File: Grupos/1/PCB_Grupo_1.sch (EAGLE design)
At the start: 45 parts, among them T1 2N7002-7-F, T2 2N7002-7-F, U1 MAX3221ECPWR, U2 ST1S14PHR, U3 MAX31855KASA+T

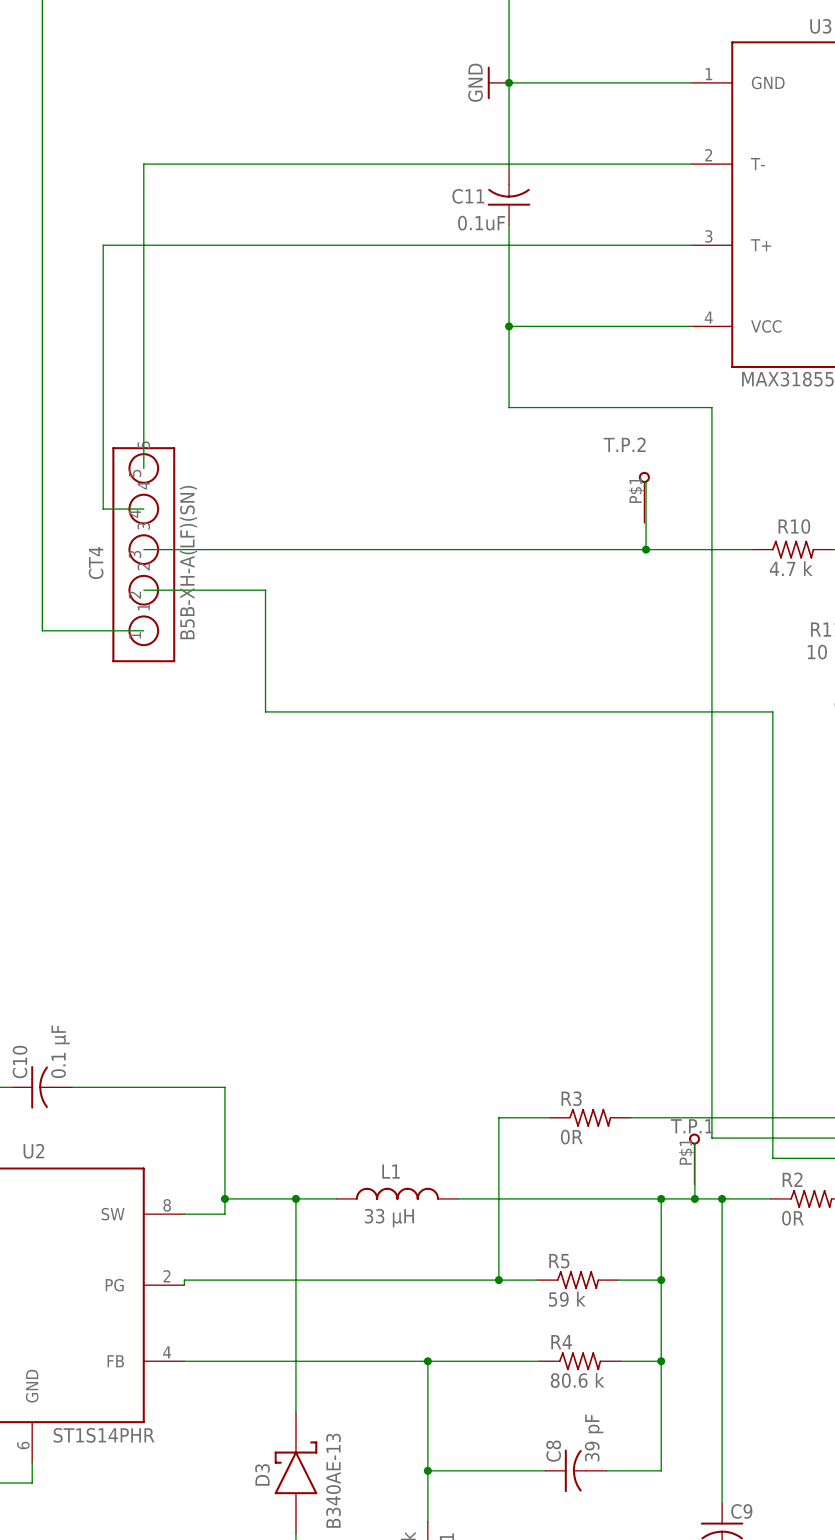
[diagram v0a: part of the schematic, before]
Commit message: Se arregla error crítico en la fuente de poder
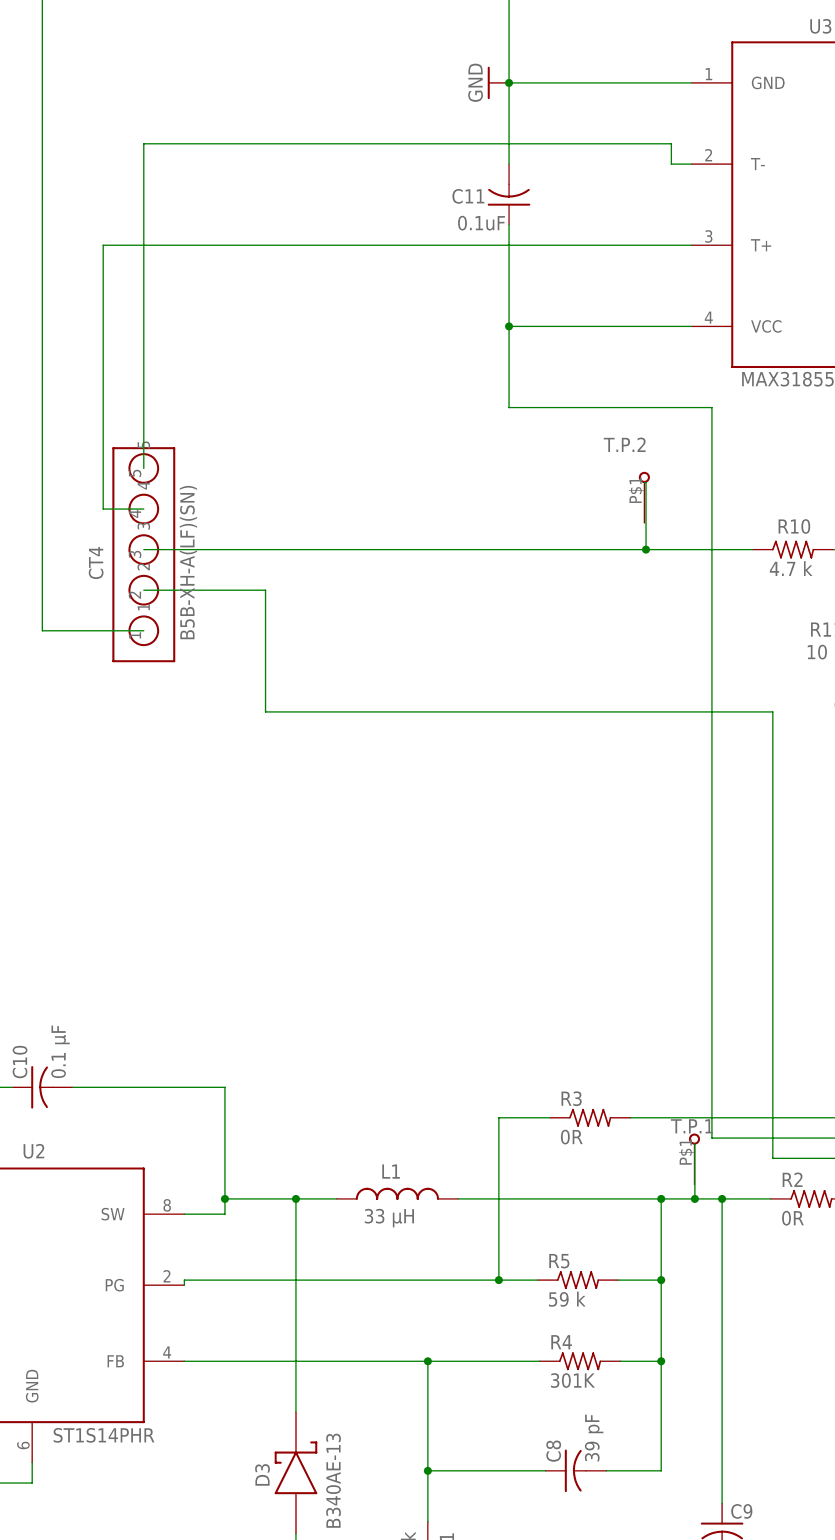
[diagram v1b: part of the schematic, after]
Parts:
- R4: value 80.6 k -> 301K; PARTNO (none) -> RC0805FR-07301KL; PART_NO RC0805FR-0780K6L -> (none)
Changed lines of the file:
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@@
 <drawing>
 <settings>
-<setting alwaysvectorfont="no"/>
+<setting alwaysvectorfont="yes"/>
 <setting verticaltext="up"/>
 </settings>
@@
 <attribute name="PART_NO" value="RC0805JR-070RL"/>
 </part>
-<part name="R4" library="rcl" library_urn="urn:adsk.eagle:library:334" deviceset="R-US_" device="R0805" package3d_urn="urn:adsk.eagle:package:23553/2" value="80.6 k">
-<spice>
-<pinmapping spiceprefix="R">
-<pinmap gate="G$1" pin="1" pinorder="1"/>
-<pinmap gate="G$1" pin="2" pinorder="2"/>
-</pinmapping>
-</spice>
-<attribute name="PART_NO" value="RC0805FR-0780K6L"/>
+<part name="R4" library="rcl" library_urn="urn:adsk.eagle:library:334" deviceset="R-US_" device="R0805" package3d_urn="urn:adsk.eagle:package:23553/2" value="301K">
+<spice>
+<pinmapping spiceprefix="R">
+<pinmap gate="G$1" pin="1" pinorder="1"/>
+<pinmap gate="G$1" pin="2" pinorder="2"/>
+</pinmapping>
+</spice>
+<attribute name="PARTNO" value="RC0805FR-07301KL"/>
 </part>
 <part name="R5" library="rcl" library_urn="urn:adsk.eagle:library:334" deviceset="R-US_" device="R0805" package3d_urn="urn:adsk.eagle:package:23553/2" value="59 k">
@@
 <attribute name="NAME" x="-170.18" y="9.1186" size="1.778" layer="95"/>
 <attribute name="VALUE" x="-170.18" y="4.318" size="1.778" layer="96"/>
-<attribute name="PART_NO" x="-166.37" y="7.62" size="0.4064" layer="96" display="off"/>
+<attribute name="PARTNO" x="-166.37" y="7.62" size="0.4064" layer="96" display="off"/>
 </instance>
 <instance part="R5" gate="G$1" x="-166.624" y="17.78" smashed="yes">
@@
 <segment>
 <pinref part="CT4" gate="CT$1" pin="5"/>
+<wire x1="-220.98" y1="119.38" x2="-220.98" y2="160.02" width="0.1524" layer="91"/>
+<wire x1="-220.98" y1="160.02" x2="-154.94" y2="160.02" width="0.1524" layer="91"/>
+<wire x1="-154.94" y1="160.02" x2="-154.94" y2="157.48" width="0.1524" layer="91"/>
 <pinref part="U3" gate="U$1" pin="T-"/>
-<wire x1="-220.98" y1="119.38" x2="-220.98" y2="157.48" width="0.1524" layer="91"/>
-<wire x1="-220.98" y1="157.48" x2="-152.4" y2="157.48" width="0.1524" layer="91"/>
-</segment>
-</net>
+<wire x1="-154.94" y1="157.48" x2="-152.4" y2="157.48" width="0.1524" layer="91"/>
+</segment>
+</net>
